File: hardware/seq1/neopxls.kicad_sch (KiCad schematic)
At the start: 51 parts, among them J10 Conn_01x04, J11 Conn_01x04, J12 Conn_01x04, J13 Conn_01x04, J14 Conn_01x04, J15 Conn_01x04, J16 Conn_01x04, J21 Conn_01x04, J22 Conn_01x04, J23 Conn_01x04, J24 Conn_01x04, J25 Conn_01x04, J26 Conn_01x04, J27 Conn_01x04, J28 Conn_01x04, J6 Conn_01x04, SW1 SW_Push_x4, SW2 SW_Push_x4, SW3 SW_Push_x4, SW4 SW_Push_x4, U2 74HC4051, U8 74HC4051

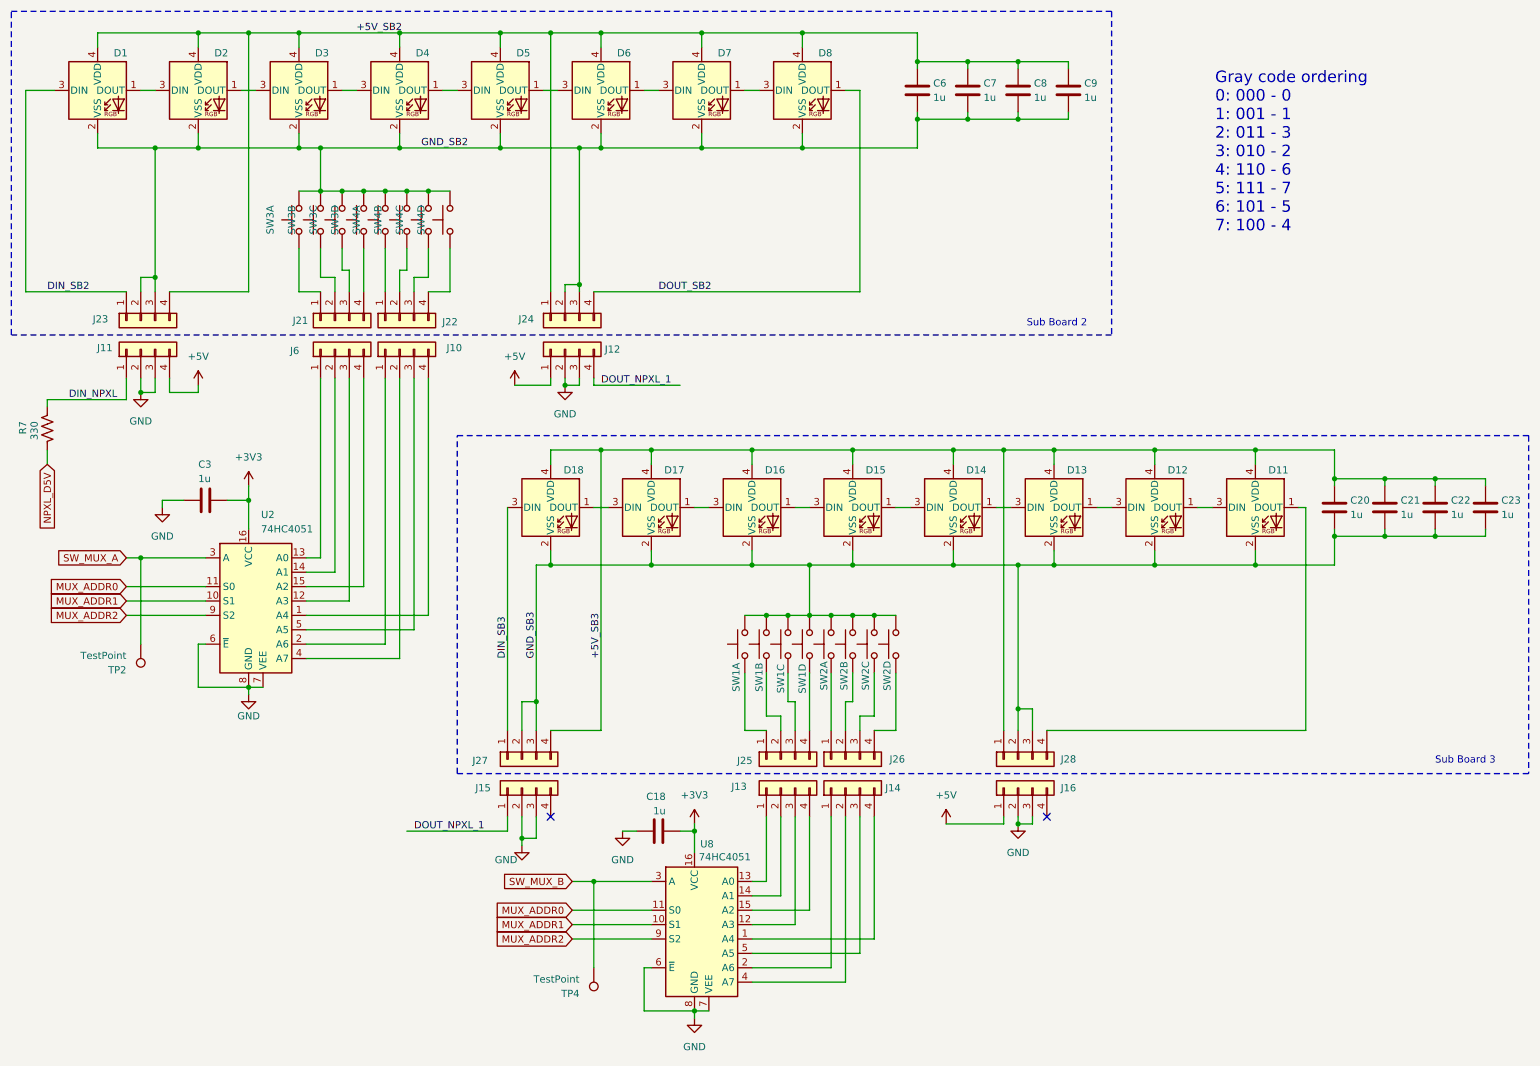
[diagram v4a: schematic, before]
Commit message: moved 1x4 keypad to separate project
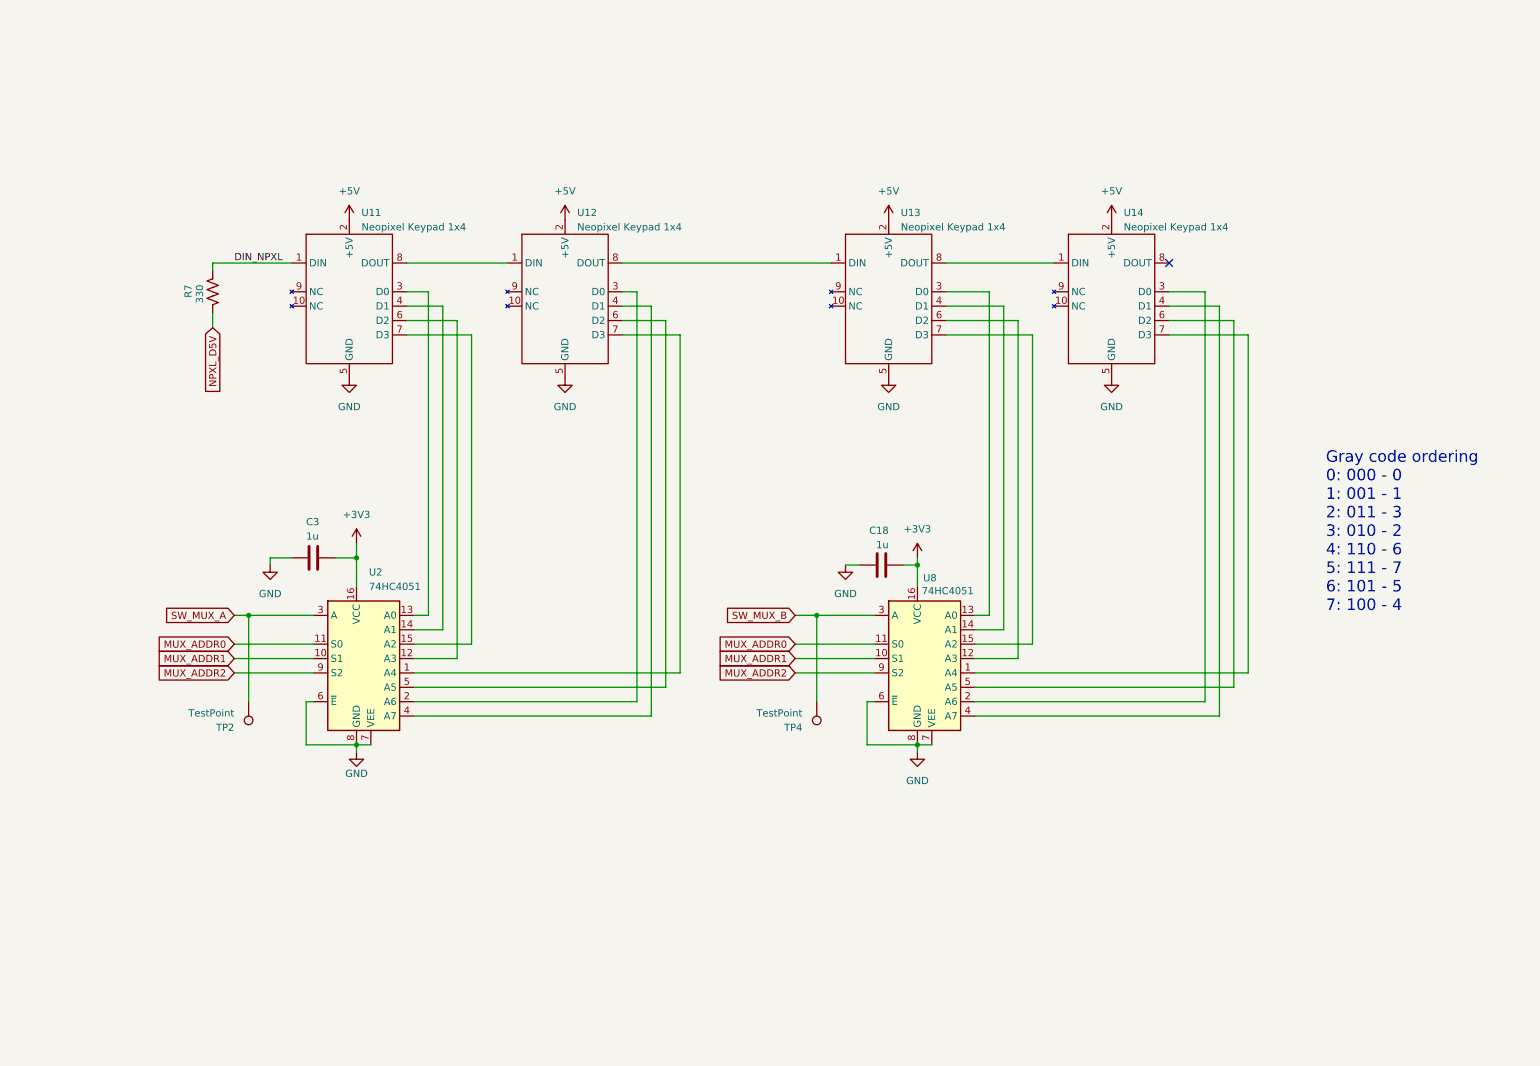
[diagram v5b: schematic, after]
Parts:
- removed C20, C21, C22, C23, C6, C7, C8, C9: 1u, Capacitor_THT:C_Disc_D5.0mm_W2.5mm_P5.00mm, symbol Device:C
- removed D1, D11, D12, D13, D14, D15, D16, D17, D18, D2, D3, D4, D5, D6, D7, D8: SK6805, LED_SMD:LED_SK6805_PLCC4_2.4x2.7mm_P1.3mm, symbol LED:SK6805
- removed J10, J11, J12, J13, J14, J15, J16, J21, J22, J23, J24, J25, J26, J27, J28, J6: Conn_01x04, Connector_PinHeader_2.54mm:PinHeader_1x04_P2.54mm_Vertical, symbol Connector_Generic:Conn_01x04
- removed SW1, SW2, SW3, SW4: SW_Push_x4, Adafruit_Trellis:SW_Silicone_Keypad_PushButton_10mm_4x1grid_NH, symbol Adafruit_Trellis:SW_Push_x4
- added U11, U12, U13, U14: Neopixel Keypad 1x4, Adafruit_Trellis:SW_Keypad_PushButton_1x4_Riser, symbol Adafruit_Trellis:SW_Neopixel_Keypad_1x4_Riser
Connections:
- net +5V: now also U11.2 (+5V), U12.2 (+5V), U13.2 (+5V), U14.2 (+5V)
- net DIN_NPXL: now also U11.1 (DIN)
- net GND: now also U11.5 (GND), U12.5 (GND), U13.5 (GND), U14.5 (GND)
- net at U8.13 (A0): now also U13.3 (D0)
- net at U8.14 (A1): now also U13.4 (D1)
- net at U8.12 (A3): now also U13.6 (D2)
- net at U8.15 (A2): now also U13.7 (D3)
- net at U2.1 (A4): now also U12.7 (D3)
- net at U2.12 (A3): now also U11.6 (D2)
- net at U2.13 (A0): now also U11.3 (D0)
- net at U2.14 (A1): now also U11.4 (D1)
- net at U2.15 (A2): now also U11.7 (D3)
- net at U2.2 (A6): now also U12.3 (D0)
- net at U2.4 (A7): now also U12.4 (D1)
- net at U2.5 (A5): now also U12.6 (D2)
- net at U8.2 (A6): now also U14.3 (D0)
- net at U8.4 (A7): now also U14.4 (D1)
- net at U8.5 (A5): now also U14.6 (D2)
- net at U8.1 (A4): now also U14.7 (D3)
- new net: U13.8 (DOUT), U14.1 (DIN)
- new net: U11.8 (DOUT), U12.1 (DIN)
- new net: U12.8 (DOUT), U13.1 (DIN)
- no-connect marks 2 -> 1
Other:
- note removed: "Sub Board 2"
- note removed: "Sub Board 3"
- moved on the sheet: C18, C3, R7, TP2, TP4, U2, U8
